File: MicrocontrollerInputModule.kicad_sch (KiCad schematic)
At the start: 49 parts, among them J1 Conn_02x04_Odd_Even, J2 IPEX 20655-045E-01, U1 W25Q16JVUXIQ, U2 RP2040, U3 MCP23017_ML, Y1 12.000MHz

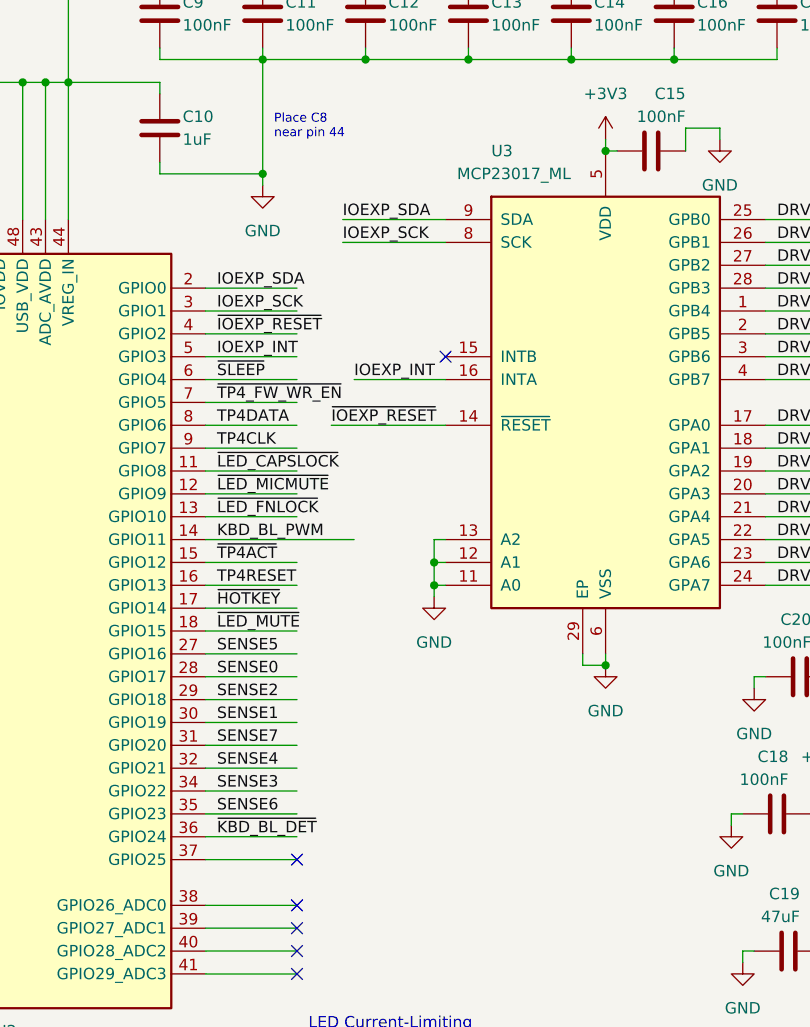
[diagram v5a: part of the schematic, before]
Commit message: Switch to 23S17 from 23017
This increases the scan rate by ~5x (from 1.7MHz clock to 10MHz) and also
works around an erratum (?) in the 23017 which forces the A7 and B7 gpios
to be outputs.  This could lead to a short circuit if (for example)
a key on the same SENSE line is held down in both the A7 and some other
row -- A7 would be driven high (because it can't be three-stated) while
the other row is driven low, and a direct connection exists through
the two key switches.

The 23S17 part requires a few extra I/O pins, but we have some to spare.
Disconnected the INT pin from the I/O expander, because the way we would
do an interrupt is by driving all low on the 23S17 pins and then watching
for a low on the RP2040 GPIOs.  We shouldn't need to trigger an interrupt
on the DRV lines from the I/O expander.  But I pulled the INT line out to
a test point just in case.
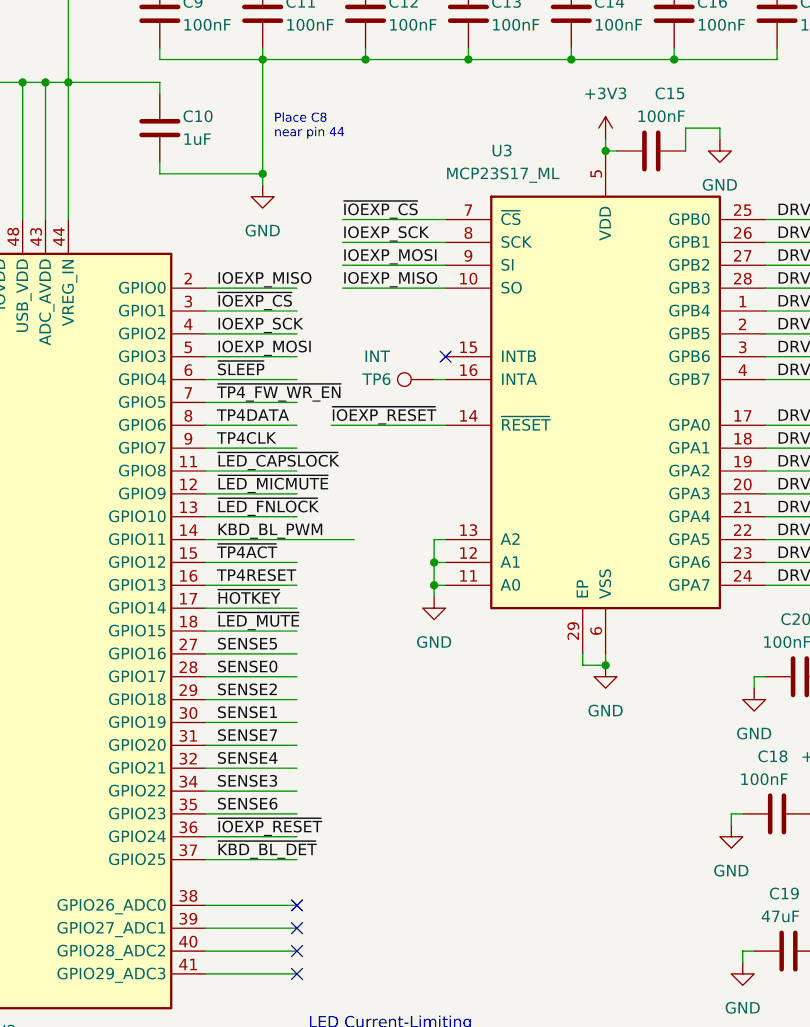
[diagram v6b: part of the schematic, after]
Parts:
- removed U3: MCP23017_ML, Package_DFN_QFN:QFN-28-1EP_6x6mm_P0.65mm_EP4.25x4.25mm, symbol Interface_Expansion:MCP23017_ML
- added TP6: INT, TestPoint:TestPoint_Pad_D1.0mm, symbol Connector:TestPoint
- added U3: MCP23S17_ML, Package_DFN_QFN:QFN-28-1EP_6x6mm_P0.65mm_EP4.25x4.25mm, symbol Interface_Expansion:MCP23S17_ML
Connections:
- net +3V3: now also U3.5 (VDD)
- net DRV0: now also U3.3 (GPB6)
- net DRV1: now also U3.28 (GPB3)
- net DRV10: now also U3.19 (GPA2)
- net DRV11: now also U3.17 (GPA0)
- net DRV12: now also U3.20 (GPA3)
- net DRV13: now also U3.22 (GPA5)
- net DRV14: now also U3.4 (GPB7)
- net DRV15: now also U3.23 (GPA6)
- net DRV2: now also U3.1 (GPB4)
- net DRV3: now also U3.27 (GPB2)
- net DRV4: now also U3.2 (GPB5)
- net DRV5: now also U3.24 (GPA7)
- net DRV6: now also U3.26 (GPB1)
- net DRV7: now also U3.25 (GPB0)
- net DRV8: now also U3.18 (GPA1)
- net DRV9: now also U3.21 (GPA4)
- net GND: now also U3.11 (A0), U3.12 (A1), U3.13 (A2), U3.29 (EP), U3.6 (VSS)
- net IOEXP_SCK: now also U2.4 (GPIO2), U3.8 (SCK); no longer U2.3 (GPIO1)
- net ~{IOEXP_RESET}: now also U2.36 (GPIO24), U3.14 (~{RESET}); no longer U2.4 (GPIO2)
- net ~{KBD_BL_DET}: now also U2.37 (GPIO25); no longer U2.36 (GPIO24)
- net IOEXP_INT renamed IOEXP_MOSI
- net IOEXP_MOSI: now also U3.9 (SI)
- net IOEXP_SDA renamed IOEXP_MISO
- net IOEXP_MISO: now also U3.10 (SO)
- new net: TP6.1, U3.16 (INTA)
- new net ~{IOEXP_CS}: U2.3 (GPIO1), U3.7 (~{CS})
- no-connect marks 7 -> 6
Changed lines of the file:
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@@
   (no_connect (at 187.96 135.89))
   (no_connect (at 187.96 133.35))
-  (no_connect (at 187.96 123.19))
   (no_connect (at 187.96 130.81))
   (no_connect (at 187.96 128.27))
@@
     (stroke (width 0) (type default))
   )
-  (wire (pts (xy 191.77 74.93) (xy 204.47 74.93))
+  (wire (pts (xy 193.04 59.69) (xy 204.47 59.69))
     (stroke (width 0) (type default))
   )
@@
     (stroke (width 0) (type default))
   )
+  (wire (pts (xy 191.77 74.93) (xy 204.47 74.93))
+    (stroke (width 0) (type default))
+  )
   (wire (pts (xy 120.65 46.99) (xy 120.65 48.26))
     (stroke (width 0) (type default))
@@
     (stroke (width 0) (type default))
   )
-  (wire (pts (xy 194.31 69.85) (xy 204.47 69.85))
+  (wire (pts (xy 193.04 57.15) (xy 204.47 57.15))
     (stroke (width 0) (type default))
   )
@@
     (stroke (width 0) (type default))
   )
+  (wire (pts (xy 203.2 69.85) (xy 204.47 69.85))
+    (stroke (width 0) (type default))
+  )
   (wire (pts (xy 85.09 115.57) (xy 88.9 115.57))
     (stroke (width 0) (type default))
@@
     (effects (font (size 1.27 1.27)) (justify left bottom))
   )
-  (label "IOEXP_SDA" (at 179.07 59.69 0) (fields_autoplaced)
+  (label "IOEXP_MISO" (at 179.07 59.69 0) (fields_autoplaced)
     (effects (font (size 1.27 1.27)) (justify left bottom))
   )
-  (label "IOEXP_INT" (at 179.07 67.31 0) (fields_autoplaced)
+  (label "IOEXP_MOSI" (at 179.07 67.31 0) (fields_autoplaced)
     (effects (font (size 1.27 1.27)) (justify left bottom))
   )
@@
     (effects (font (size 1.27 1.27)) (justify left bottom))
   )
-  (label "IOEXP_INT" (at 194.31 69.85 0) (fields_autoplaced)
+  (label "IOEXP_MOSI" (at 193.04 57.15 0) (fields_autoplaced)
     (effects (font (size 1.27 1.27)) (justify left bottom))
   )
@@
     (effects (font (size 1.27 1.27)) (justify left bottom))
   )
-  (label "~{KBD_BL_DET}" (at 179.07 120.65 0) (fields_autoplaced)
+  (label "~{KBD_BL_DET}" (at 179.07 123.19 0) (fields_autoplaced)
     (effects (font (size 1.27 1.27)) (justify left bottom))
   )
@@
     (effects (font (size 1.27 1.27)) (justify right bottom))
   )
-  (label "IOEXP_SCK" (at 179.07 62.23 0) (fields_autoplaced)
+  (label "~{IOEXP_CS}" (at 179.07 62.23 0) (fields_autoplaced)
     (effects (font (size 1.27 1.27)) (justify left bottom))
   )
-  (label "IOEXP_SDA" (at 193.04 52.07 0) (fields_autoplaced)
+  (label "~{IOEXP_CS}" (at 193.04 52.07 0) (fields_autoplaced)
     (effects (font (size 1.27 1.27)) (justify left bottom))
   )
@@
     (effects (font (size 1.27 1.27)) (justify left bottom))
   )
-  (label "~{IOEXP_RESET}" (at 179.07 64.77 0) (fields_autoplaced)
+  (label "IOEXP_SCK" (at 179.07 64.77 0) (fields_autoplaced)
     (effects (font (size 1.27 1.27)) (justify left bottom))
   )
@@
     (effects (font (size 1.27 1.27)) (justify left bottom))
   )
+  (label "~{IOEXP_RESET}" (at 191.77 74.93 0) (fields_autoplaced)
+    (effects (font (size 1.27 1.27)) (justify left bottom))
+  )
   (label "~{LED_FNLOCK}" (at 179.07 85.09 0) (fields_autoplaced)
     (effects (font (size 1.27 1.27)) (justify left bottom))
@@
     (effects (font (size 1.27 1.27)) (justify left bottom))
   )
+  (label "~{IOEXP_RESET}" (at 179.07 120.65 0) (fields_autoplaced)
+    (effects (font (size 1.27 1.27)) (justify left bottom))
+  )
   (label "KBD_BL_PWM" (at 179.07 87.63 0) (fields_autoplaced)
     (effects (font (size 1.27 1.27)) (justify left bottom))
@@
     (effects (font (size 1.27 1.27)) (justify left bottom))
   )
-  (label "~{IOEXP_RESET}" (at 191.77 74.93 0) (fields_autoplaced)
+  (label "IOEXP_MISO" (at 193.04 59.69 0) (fields_autoplaced)
     (effects (font (size 1.27 1.27)) (justify left bottom))
   )
@@
     )
   )
-  (symbol (lib_id "Interface_Expansion:MCP23017_ML") (at 222.25 72.39 0) (unit 1)
-    (in_bom yes) (on_board yes) (dnp no)
-    (property "Reference" "U3" (at 209.55 44.45 0)
-      (effects (font (size 1.27 1.27)) (justify left))
-    )
-    (property "Value" "MCP23017_ML" (at 205.74 46.99 0)
-      (effects (font (size 1.27 1.27)) (justify left))
-    )
-    (property "Footprint" "Package_DFN_QFN:QFN-28-1EP_6x6mm_P0.65mm_EP4.25x4.25mm" (at 227.33 97.79 0)
-      (effects (font (size 1.27 1.27)) (justify left) hide)
-    )
-    (property "Datasheet" "http://ww1.microchip.com/downloads/en/DeviceDoc/20001952C.pdf" (at 227.33 100.33 0)
-      (effects (font (size 1.27 1.27)) (justify left) hide)
-    )
-    (pin "23")
-    (pin "8")
-    (pin "4")
-    (pin "21")
-    (pin "5")
-    (pin "24")
-    (pin "9")
-    (pin "18")
-    (pin "29")
-    (pin "17")
-    (pin "26")
-    (pin "19")
-    (pin "2")
-    (pin "6")
-    (pin "25")
-    (pin "20")
-    (pin "27")
-    (pin "22")
-    (pin "16")
-    (pin "11")
-    (pin "12")
-    (pin "15")
-    (pin "13")
-    (pin "3")
-    (pin "28")
-    (pin "7")
-    (pin "14")
-    (pin "10")
-    (pin "1")
-    (instances
-      (project "MicrocontrollerInputModule"
-        (path "/e1225fe3-1add-4bf0-8592-1d94311392e6"
-          (reference "U3") (unit 1)
-        )
-      )
-    )
-  )
   (symbol (lib_id "Connector:TestPoint") (at 53.34 111.76 90) (unit 1)
     (in_bom yes) (on_board yes) (dnp no)
@@
     )
   )
+  (symbol (lib_id "Interface_Expansion:MCP23S17_ML") (at 222.25 72.39 0) (unit 1)
+    (in_bom yes) (on_board yes) (dnp no)
+    (property "Reference" "U3" (at 209.55 44.45 0)
+      (effects (font (size 1.27 1.27)) (justify left))
+    )
+    (property "Value" "MCP23S17_ML" (at 204.47 46.99 0)
+      (effects (font (size 1.27 1.27)) (justify left))
+    )
+    (property "Footprint" "Package_DFN_QFN:QFN-28-1EP_6x6mm_P0.65mm_EP4.25x4.25mm" (at 227.33 97.79 0)
+      (effects (font (size 1.27 1.27)) (justify left) hide)
+    )
+    (property "Datasheet" "http://ww1.microchip.com/downloads/en/DeviceDoc/20001952C.pdf" (at 227.33 100.33 0)
+      (effects (font (size 1.27 1.27)) (justify left) hide)
+    )
+    (pin "7")
+    (pin "23")
+    (pin "17")
+    (pin "13")
+    (pin "26")
+    (pin "27")
+    (pin "28")
+    (pin "25")
+    (pin "24")
+    (pin "9")
+    (pin "2")
+    (pin "10")
+    (pin "21")
+    (pin "29")
+    (pin "3")
+    (pin "16")
+    (pin "14")
+    (pin "4")
+    (pin "20")
+    (pin "22")
+    (pin "5")
+    (pin "15")
+    (pin "12")
+    (pin "6")
+    (pin "11")
+    (pin "8")
+    (pin "19")
+    (pin "18")
+    (pin "1")
+    (instances
+      (project "MicrocontrollerInputModule"
+        (path "/e1225fe3-1add-4bf0-8592-1d94311392e6"
+          (reference "U3") (unit 1)
+        )
+      )
+    )
+  )
   (symbol (lib_id "power:GND") (at 152.4 147.32 0) (unit 1)
     (in_bom yes) (on_board yes) (dnp no) (fields_autoplaced)
@@
         )
       )
+    )
+  )
+  (symbol (lib_id "Connector:TestPoint") (at 203.2 69.85 90) (unit 1)
+    (in_bom yes) (on_board yes) (dnp no)
+    (property "Reference" "TP6" (at 196.85 69.85 90)
+      (effects (font (size 1.27 1.27)))
+    )
+    (property "Value" "INT" (at 196.85 67.31 90)
+      (effects (font (size 1.27 1.27)))
+    )
+    (property "Footprint" "TestPoint:TestPoint_Pad_D1.0mm" (at 203.2 64.77 0)
+      (effects (font (size 1.27 1.27)) hide)
+    )
+    (property "Datasheet" "~" (at 203.2 64.77 0)
+      (effects (font (size 1.27 1.27)) hide)
+    )
+    (pin "1")
+    (instances
+      (project "MicrocontrollerInputModule"
+        (path "/e1225fe3-1add-4bf0-8592-1d94311392e6"
+          (reference "TP6") (unit 1)
+        )
+      )

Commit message: Update with BOM information
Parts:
- C1, C11, C12, C13, C14, C15, C16, C17, C18, C20, C4, C6, C9: Digikey (none) -> 1276-1001-1-ND; LCSC (none) -> C1525; MANUFACTURER (none) -> Samsung; MP (none) -> CL05B104KO5NNNC
- C10, C7: Digikey (none) -> 1276-1445-1-ND; LCSC (none) -> C52923; MANUFACTURER (none) -> Samsung; MP (none) -> CL05A105KA5NQNC
- C19: footprint Capacitor_SMD:C_0603_1608Metric -> Capacitor_SMD:C_0805_2012Metric; Digikey (none) -> 1276-1852-1-ND; LCSC (none) -> C16780; MANUFACTURER (none) -> Samsung; MP (none) -> CL21A476MQYNNNE
- C2, C3: Digikey (none) -> 490-5888-1-ND; LCSC (none) -> C1555; LCSC Alt (none) -> C1548; MANUFACTURER (none) -> Murata; MP (none) -> GRM1555C1H150JA01D
- C5, C8: Digikey (none) -> 1276-1869-1-ND; LCSC (none) -> C96446; MANUFACTURER (none) -> Samsung; MP (none) -> CL10A106MA8NRNC
- D1, D2, D3, D4, D5: Digikey (none) -> F9744CT-ND; LCSC (none) -> C468904; MANUFACTURER (none) -> Littelfuse; MP (none) -> SP0402B-ULC-01ETG
- H1, H2: Digikey (none) -> 36-24929CT-ND; LCSC (none) -> C5354888; MANUFACTURER (none) -> Keystone; MP (none) -> 24929
- J2: Digikey (none) -> 5378-20655-045E-01CT-ND; LCSC (none) -> C2919534; LCSC Alt (none) -> missing
- R1, R3: Digikey (none) -> 311-1.00KLRCT-ND; LCSC (none) -> C11702; MANUFACTURER (none) -> Yageo; MP (none) -> RC0402FR-071KL
- R4, R5: Digikey (none) -> P27.0LCT-ND; LCSC (none) -> C138021; MANUFACTURER (none) -> Panasonic; MP (none) -> ERJ-2RKF27R0X
- R6, R7, R8, R9: Digikey (none) -> P100LCT-ND; LCSC (none) -> C25076; MANUFACTURER (none) -> Panasonic; MP (none) -> ERJ-2RKF1000X
- U1: Digikey (none) -> 256-W25Q16JVUXIQTRCT-ND; LCSC (none) -> C2843335; MANUFACTURER (none) -> Winbond; MP (none) -> W25Q16JVUXIQ
- U2: Digikey (none) -> 2648-SC0914(13)CT-ND; LCSC (none) -> C2040; MANUFACTURER (none) -> Raspberry Pi; MP (none) -> RP2040
- U3: Digikey (none) -> MCP23S17T-E/MLCT-ND; LCSC (none) -> C629442; MANUFACTURER (none) -> Microchip Technology; MP (none) -> MCP23S17T-E/ML
- Y1: Digikey (none) -> 535-10261-1-ND; LCSC (none) -> C9002; LCSC Alt (none) -> C5360391; MANUFACTURER (none) -> Abracon; MP (none) -> ABM8G-12.000MHZ-18-D2Y-T
